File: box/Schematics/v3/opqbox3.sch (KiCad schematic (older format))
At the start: 2 parts, among them J1 Conn_01x02_Male, J2 Conn_01x02_Male

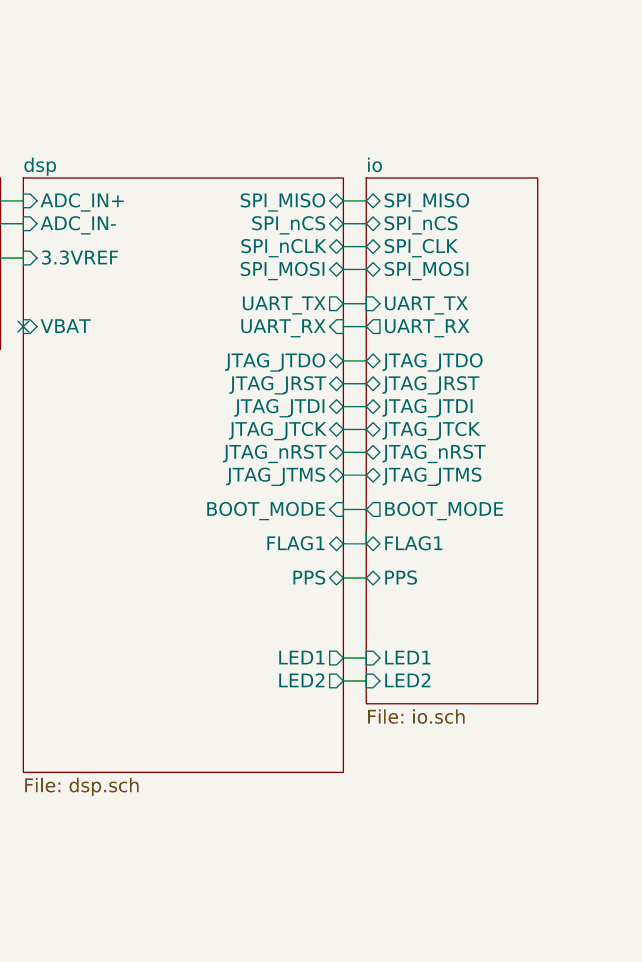
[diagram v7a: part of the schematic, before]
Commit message: add chip pro and battery
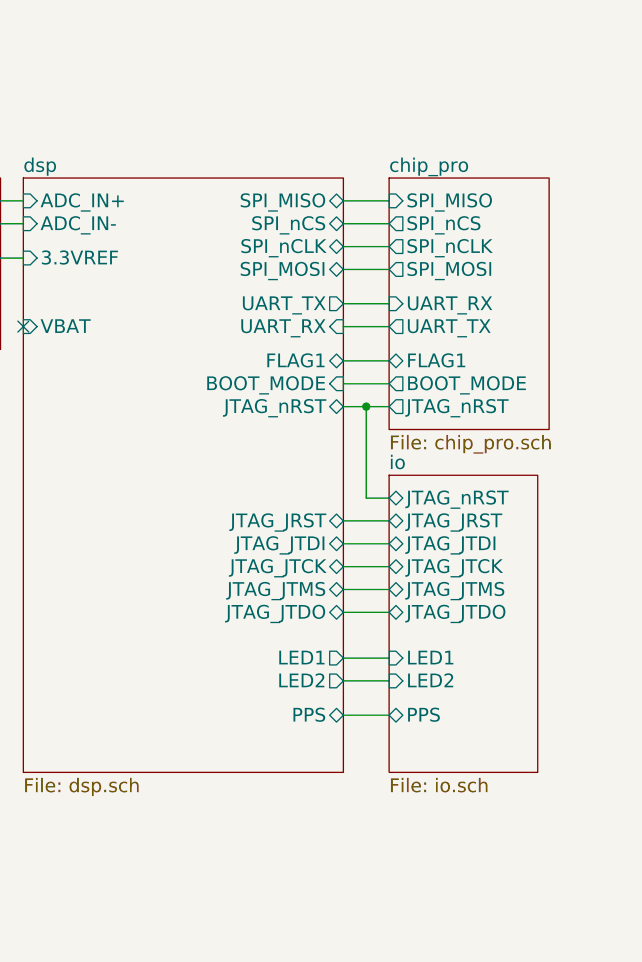
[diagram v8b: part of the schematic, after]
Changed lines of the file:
@@
 EESchema Schematic File Version 2
-LIBS:opqbox3-rescue
 LIBS:opqbox3
 LIBS:device
@@
 $Descr A4 11693 8268
 encoding utf-8
-Sheet 1 4
+Sheet 1 5
 Title ""
 Date ""
@@
 NOT isolated
 $Sheet
-S 4850 1200 750  2300
-U 5A8506F3
-F0 "io" 60
-F1 "io.sch" 60
-F2 "SPI_MISO" B L 4850 1300 60
-F3 "SPI_MOSI" B L 4850 1600 60
-F4 "SPI_nCS" B L 4850 1400 60
-F5 "SPI_CLK" B L 4850 1500 60
-F6 "JTAG_nRST" B L 4850 2400 60
-F7 "BOOT_MODE" O L 4850 2650 60
-F8 "UART_RX" O L 4850 1850 60
-F9 "UART_TX" I L 4850 1750 60
-F10 "FLAG1" B L 4850 2800 60
-F11 "JTAG_JRST" B L 4850 2100 60
-F12 "JTAG_JTCK" B L 4850 2300 60
-F13 "JTAG_JTDI" B L 4850 2200 60
-F14 "JTAG_JTDO" B L 4850 2000 60
-F15 "JTAG_JTMS" B L 4850 2500 60
-F16 "PPS" B L 4850 2950 60
-F17 "LED1" I L 4850 3300 60
-F18 "LED2" I L 4850 3400 60
-$EndSheet
-$Sheet
 S 3350 1200 1400 2600
 U 5A835DDE
 F0 "dsp" 60
 F1 "dsp.sch" 60
-F2 "BOOT_MODE" I R 4750 2650 60
+F2 "BOOT_MODE" I R 4750 2100 60
 F3 "VBAT" I L 3350 1850 60
 F4 "SPI_MISO" B R 4750 1300 60
 F5 "LED1" O R 4750 3300 60
-F6 "FLAG1" B R 4750 2800 60
+F6 "FLAG1" B R 4750 2000 60
 F7 "ADC_IN+" I L 3350 1300 60
 F8 "SPI_nCS" B R 4750 1400 60
@@
 F11 "ADC_IN-" I L 3350 1400 60
 F12 "LED2" O R 4750 3400 60
-F13 "JTAG_JTDO" B R 4750 2000 60
-F14 "JTAG_JRST" B R 4750 2100 60
-F15 "JTAG_JTDI" B R 4750 2200 60
-F16 "JTAG_JTCK" B R 4750 2300 60
-F17 "JTAG_nRST" B R 4750 2400 60
-F18 "JTAG_JTMS" B R 4750 2500 60
+F13 "JTAG_JTDO" B R 4750 3100 60
+F14 "JTAG_JRST" B R 4750 2700 60
+F15 "JTAG_JTDI" B R 4750 2800 60
+F16 "JTAG_JTCK" B R 4750 2900 60
+F17 "JTAG_nRST" B R 4750 2200 60
+F18 "JTAG_JTMS" B R 4750 3000 60
 F19 "3.3VREF" I L 3350 1550 60
 F20 "UART_RX" I R 4750 1850 60
 F21 "UART_TX" O R 4750 1750 60
-F22 "PPS" B R 4750 2950 60
+F22 "PPS" B R 4750 3550 60
 $EndSheet
 Wire Notes Line
@@
 Connection ~ 1900 1350
 Wire Wire Line
-	4850 2750 4850 2800
-Wire Wire Line
-	4850 2800 4750 2800
-Wire Wire Line
-	4750 2650 4850 2650
-Wire Wire Line
-	4750 2500 4850 2500
-Wire Wire Line
-	4750 2400 4850 2400
-Wire Wire Line
-	4750 2300 4850 2300
-Wire Wire Line
-	4750 2200 4850 2200
-Wire Wire Line
-	4750 2100 4850 2100
-Wire Wire Line
-	4750 2000 4850 2000
-Wire Wire Line
-	4750 1850 4850 1850
-Wire Wire Line
-	4850 1750 4750 1750
-Wire Wire Line
-	4750 1600 4850 1600
-Wire Wire Line
-	4750 1500 4850 1500
-Wire Wire Line
-	4750 1400 4850 1400
-Wire Wire Line
-	4750 1300 4850 1300
-Wire Wire Line
-	4750 2950 4850 2950
+	4750 2800 4950 2800
+Wire Wire Line
+	4750 1850 4950 1850
+Wire Wire Line
+	4750 1750 4950 1750
+Wire Wire Line
+	4750 1600 4950 1600
+Wire Wire Line
+	4750 1500 4950 1500
+Wire Wire Line
+	4750 1400 4950 1400
+Wire Wire Line
+	4750 1300 4950 1300
 Wire Wire Line
 	3250 1300 3350 1300
@@
 	3250 1550 3350 1550
 Wire Wire Line
-	4750 3300 4850 3300
-Wire Wire Line
-	4750 3400 4850 3400
+	4750 3300 4950 3300
+Wire Wire Line
+	4750 3400 4950 3400
 NoConn ~ 3350 1850
 $Comp
@@
 	1700 1650 1700 1750
 Connection ~ 1700 1750
+$Sheet
+S 4950 1200 700  1100
+U 5A9ABA19
+F0 "chip_pro" 60
+F1 "chip_pro.sch" 60
+F2 "SPI_MOSI" O L 4950 1600 60
+F3 "SPI_MISO" I L 4950 1300 60
+F4 "SPI_nCS" O L 4950 1400 60
+F5 "SPI_nCLK" O L 4950 1500 60
+F6 "UART_TX" O L 4950 1850 60
+F7 "UART_RX" I L 4950 1750 60
+F8 "BOOT_MODE" O L 4950 2100 60
+F9 "FLAG1" B L 4950 2000 60
+F10 "JTAG_nRST" O L 4950 2200 60
+$EndSheet
+$Sheet
+S 4950 2500 650  1300
+U 5A8506F3
+F0 "io" 60
+F1 "io.sch" 60
+F2 "JTAG_JRST" B L 4950 2700 60
+F3 "JTAG_JTCK" B L 4950 2900 60
+F4 "JTAG_JTDI" B L 4950 2800 60
+F5 "JTAG_JTDO" B L 4950 3100 60
+F6 "JTAG_JTMS" B L 4950 3000 60
+F7 "PPS" B L 4950 3550 60
+F8 "LED1" I L 4950 3300 60
+F9 "LED2" I L 4950 3400 60
+F10 "JTAG_nRST" B L 4950 2600 60
+$EndSheet
+Wire Wire Line
+	4750 2900 4950 2900
+Wire Wire Line
+	4750 2700 4950 2700
+Wire Wire Line
+	4750 3000 4950 3000
+Wire Wire Line
+	4750 2000 4950 2000
+Wire Wire Line
+	4750 2100 4950 2100
+Wire Wire Line
+	4750 2200 4950 2200
+Wire Wire Line
+	4750 3100 4950 3100
+Wire Wire Line
+	4750 3550 4950 3550
+Wire Wire Line
+	4850 2200 4850 2600
+Wire Wire Line
+	4850 2600 4950 2600
+Connection ~ 4850 2200
 $EndSCHEMATC
